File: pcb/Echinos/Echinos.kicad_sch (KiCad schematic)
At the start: 55 parts, among them J1 Conn_01x06_Socket, J10 TagConnect_6pins, J2 Conn_01x06_Socket, J3 Conn_01x06_Socket, J5 Conn_01x05_Socket, J6 USB_B_Micro, J7 Conn_01x04_Socket, J8 USB_C_Receptacle_USB2.0, J9 Conn_01x03_Socket, SW3 Reset, SW4 Reset, U1 Helios, U2 USBLC6-2P6, U3 XC6210B332MR-G, U7 USBLC6-2P6, U8 74LVC1T45

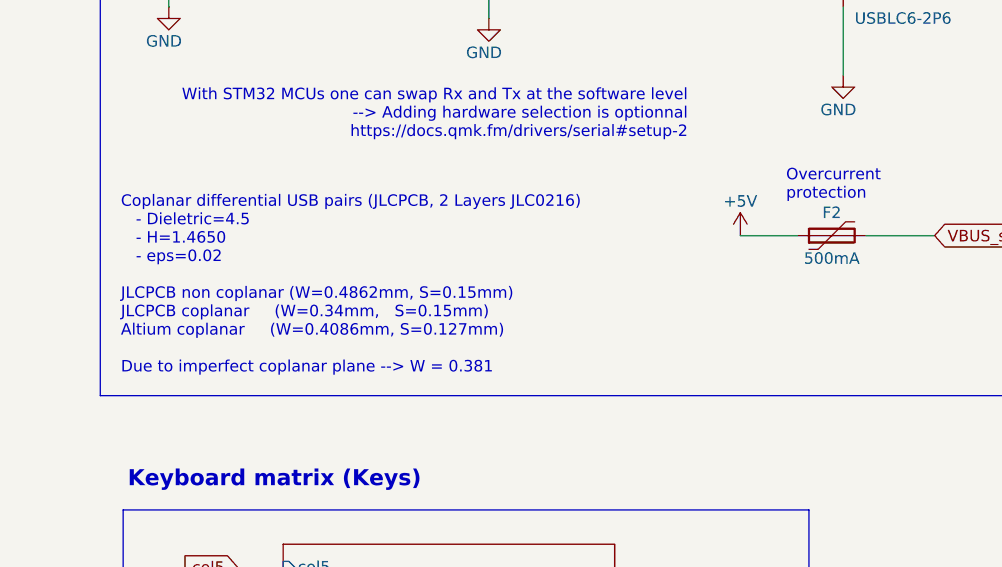
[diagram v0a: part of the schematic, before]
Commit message: [PCB] - Save last state with on board RP2040.   - Route crystal and 1V1
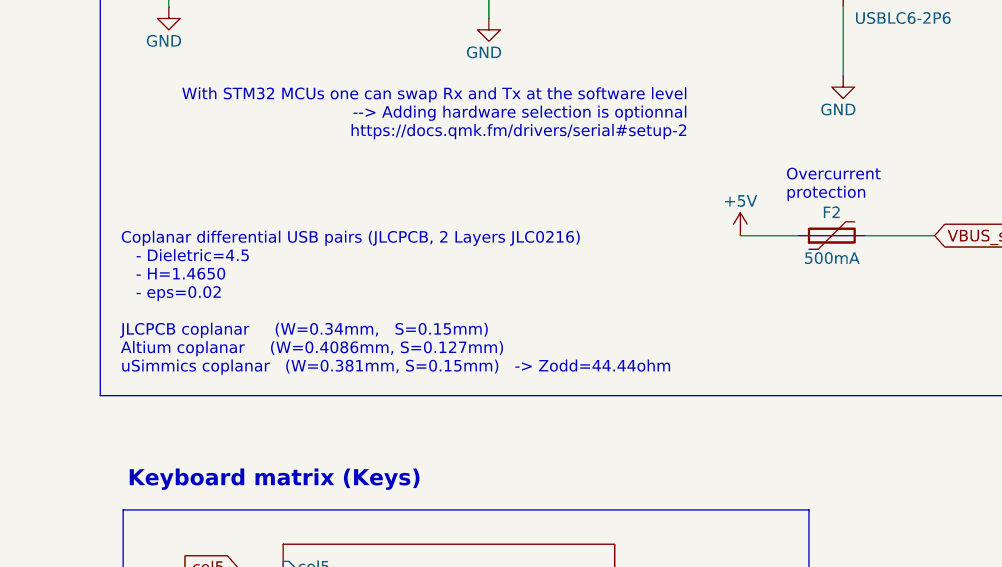
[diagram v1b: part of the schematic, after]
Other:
- note added: "Coplanar differential USB pairs (JLCPCB, 2 Layers JLC0216) - Dieletric=4.5 - H=1.4650 - eps=0.02 JLCPCB coplanar (W=0.34mm, S=0.15mm) Altium coplanar (W=0.4086mm, S=0.127mm) uSimmics coplanar (W=0.381mm, S=0.15mm) -> Zodd=44.44ohm"
- note removed: "Coplanar differential USB pairs (JLCPCB, 2 Layers JLC0216) - Dieletric=4.5 - H=1.4650 - eps=0.02 JLCPCB non coplanar (W=0.4862mm, S=0.15mm) JLCPCB coplanar (W=0.34mm, S=0.15mm) Altium coplanar (W=0.4086mm, S=0.127mm) Due to imperfect coplanar plane --> W = 0.381"
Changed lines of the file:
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@@
 		)
 	)
-	(text "Coplanar differential USB pairs (JLCPCB, 2 Layers JLC0216)\n   - Dieletric=4.5\n   - H=1.4650\n   - eps=0.02\n\nJLCPCB non coplanar (W=0.4862mm, S=0.15mm)\nJLCPCB coplanar     (W=0.34mm,   S=0.15mm)\nAltium coplanar     (W=0.4086mm, S=0.127mm)\n\nDue to imperfect coplanar plane --> W = 0.381"
+	(text "Coplanar differential USB pairs (JLCPCB, 2 Layers JLC0216)\n   - Dieletric=4.5\n   - H=1.4650\n   - eps=0.02\n\nJLCPCB coplanar     (W=0.34mm,   S=0.15mm)\nAltium coplanar     (W=0.4086mm, S=0.127mm) \nuSimmics coplanar   (W=0.381mm, S=0.15mm)   -> Zodd=44.44ohm"
 		(exclude_from_sim no)
 		(at 21.336 101.854 0)

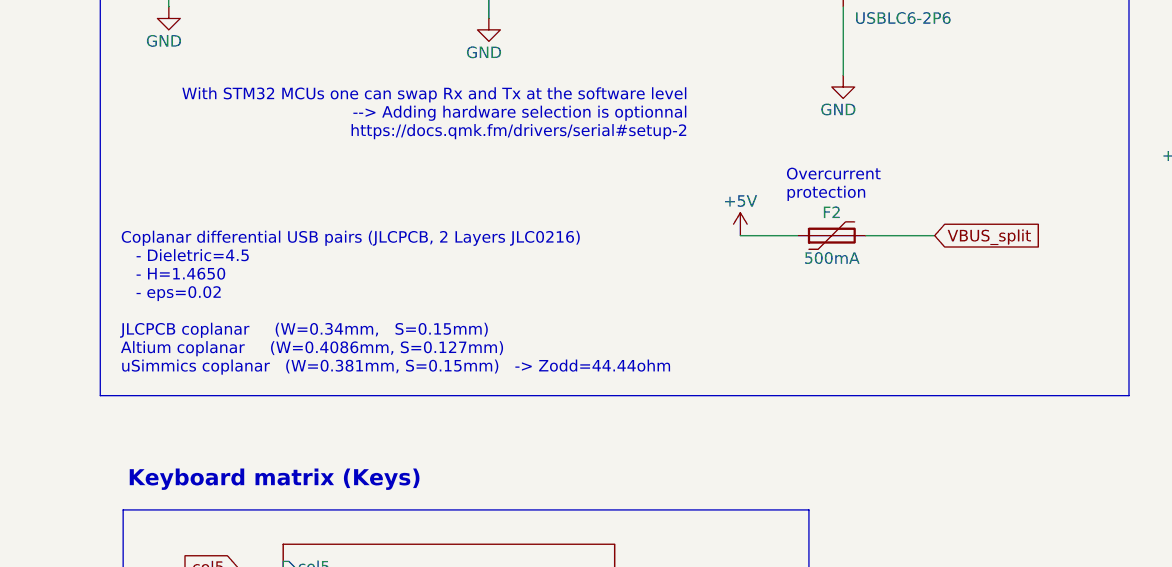
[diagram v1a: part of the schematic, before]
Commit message: [PCB] - Save last state with on board RP2040.   - Correct USB impedance   - Improve top plane grounding   - Add via at each layer switch   - Fix ERC issues   - Fix orientation / position of silkscreen
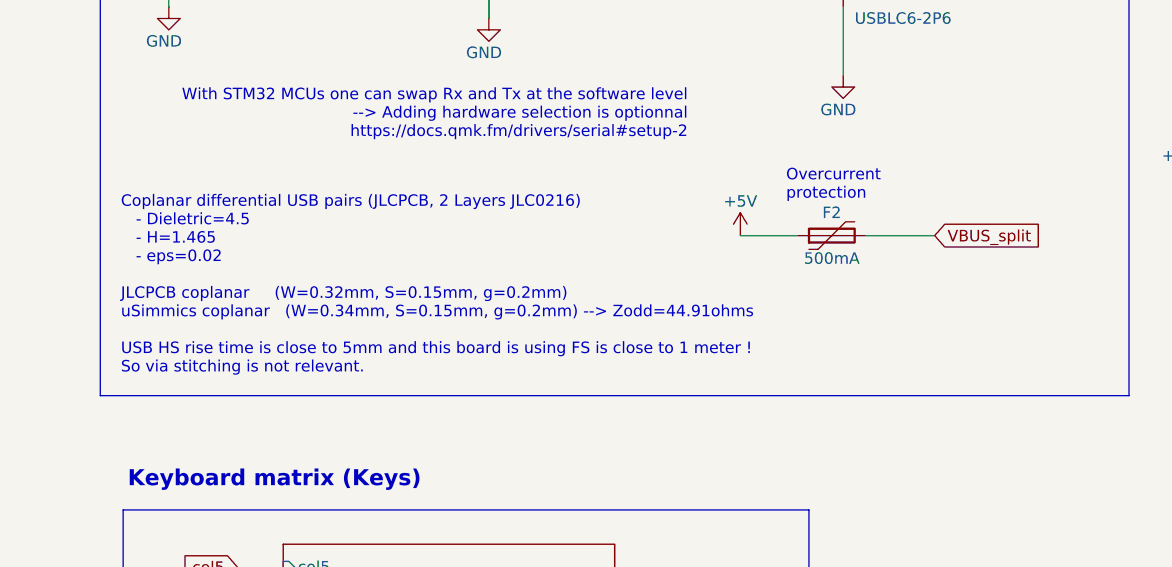
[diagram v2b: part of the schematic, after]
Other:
- note added: "Coplanar differential USB pairs (JLCPCB, 2 Layers JLC0216) - Dieletric=4.5 - H=1.465 - eps=0.02 JLCPCB coplanar (W=0.32mm, S=0.15mm, g=0.2mm) uSimmics coplanar (W=0.34mm, S=0.15mm, g=0.2mm) --> Zodd=44.91ohms USB HS rise time is close to 5mm and this board is using FS is close to 1 meter ! So via stitching is not relevant."
- note removed: "Coplanar differential USB pairs (JLCPCB, 2 Layers JLC0216) - Dieletric=4.5 - H=1.4650 - eps=0.02 JLCPCB coplanar (W=0.34mm, S=0.15mm) Altium coplanar (W=0.4086mm, S=0.127mm) uSimmics coplanar (W=0.381mm, S=0.15mm) -> Zodd=44.44ohm"
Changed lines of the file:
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@@
 		)
 	)
-	(text "Coplanar differential USB pairs (JLCPCB, 2 Layers JLC0216)\n   - Dieletric=4.5\n   - H=1.4650\n   - eps=0.02\n\nJLCPCB coplanar     (W=0.34mm,   S=0.15mm)\nAltium coplanar     (W=0.4086mm, S=0.127mm) \nuSimmics coplanar   (W=0.381mm, S=0.15mm)   -> Zodd=44.44ohm"
+	(text "Coplanar differential USB pairs (JLCPCB, 2 Layers JLC0216)\n   - Dieletric=4.5\n   - H=1.465\n   - eps=0.02\n\nJLCPCB coplanar     (W=0.32mm, S=0.15mm, g=0.2mm)\nuSimmics coplanar   (W=0.34mm, S=0.15mm, g=0.2mm) --> Zodd=44.91ohms\n\nUSB HS rise time is close to 5mm and this board is using FS is close to 1 meter !\nSo via stitching is not relevant."
 		(exclude_from_sim no)
 		(at 21.336 101.854 0)

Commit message: [PCB] - Save last state with on board RP2040.   - Clean schematics   - Fix flash capacitor value   - Fix flash schema to match all footprint pins   - Pass ERC (schema and pcb)   - Select missing LCSC components (USBC/B, buttons, vik connector)   - Add more margin to lateral pads in USB B footprint   - Improve top plane grounding under switches   - Adjust orientation and position to match JLCPCB   - Clean unused fields in schematics   - Add VIK connector footprint to lib (updated to match more models)   - Harmonization of footprints packaging for caps and resistors (either 0805 or 0402)   - Check availability and correctness of all parts   - Fix space in fields (was LCSC2 on leds)
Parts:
- removed J10: TagConnect_6pins, Connector:Tag-Connect_TC2030-IDC-FP_2x03_P1.27mm_Vertical, symbol Connector:Conn_ARM_SWD_TagConnect_TC2030
- removed J9: Conn_01x03_Socket, Connector_JST:JST_SH_BM03B-SRSS-TB_1x03-1MP_P1.00mm_Vertical, symbol Connector:Conn_01x03_Pin
- removed R18, R19: 100, Resistor_SMD:R_0805_2012Metric, symbol Device:R
- removed S2, S3, S4, S5, S6: GasketSupport, Echinos:EarCut_8mm, symbol Mechanical:Mechanical_Shape
- removed SW3, SW4: Reset, Button_Switch_SMD:SW_SPST_TS-1088-xR020, symbol Switch:SW_Push
- removed U1: Helios, Echinos:Helios_AH_USBup, symbol PCM_marbastlib-promicroish:Helios
- C1: value 1µ -> 1u; footprint Capacitor_SMD:C_0603_1608Metric_Pad1.08x0.95mm_HandSolder -> Capacitor_SMD:C_0805_2012Metric; LCSC C458913 -> C24123
- C2: value 4.7µ -> 1u; footprint Capacitor_SMD:C_0603_1608Metric_Pad1.08x0.95mm_HandSolder -> Capacitor_SMD:C_0805_2012Metric; LCSC C19666 -> C24123
- C3: MPN  10uF 20% 10V 0805 -> (none)
- D1: footprint Diode_SMD:D_SOD-323_HandSoldering -> LED_SMD:LED_0805_2012Metric; LCSC (none) -> C84260
- D3: MPN  B5817WS -> (none)
- FB1: MPN  BLM21AG601SH1D -> (none)
- J4: footprint Connector_FFC-FPC:Hirose_FH12-12S-0.5SH_1x12-1MP_P0.50mm_Horizontal -> Echinos:vik-keyboard-connector-horizontal; LCSC2 C3446010 -> C2906115; LCSC2_old_ (none) -> C3446010; LCSC_old (none) -> C479750
- J5: now left out of the parts list
- J6: Datasheet2 (none) -> https://www.lcsc.com/datasheet/C132562.pdf; Datasheet2_bis (none) -> https://fr.aliexpress.com/item/1005001673927357.html; Datasheet_bis (none) -> https://fr.aliexpress.com/item/1005007360060905.html; FT Position Offset (none) -> 0, 0.45; LCSC (none) -> C456008; LCSC2 (none) -> C132562
- J8: symbol Connector:USB_C_Receptacle_USB2.0 -> Connector:USB_C_Receptacle_USB2.0_16P; LCSC ??? C963373 ??? -> C3025063; MPN  ??? USB4510-03-1-A ??? -> (none)
- R12: MPN  5.1k 1% 0402 -> (none)
- R13, R14, R15, R16: footprint Resistor_SMD:R_0805_2012Metric_Pad1.20x1.40mm_HandSolder -> Resistor_SMD:R_0805_2012Metric
- R7, R8: MPN  5.1k 1% 0805 -> (none)
- R9: footprint Resistor_SMD:R_0402_1005Metric_Pad0.72x0.64mm_HandSolder -> Resistor_SMD:R_0805_2012Metric; LCSC C11702 -> C17513
- U2, U7: FT Rotation Offset (none) -> 90; MPN  USBLC6-2SC6 -> (none)
- U8: footprint Package_TO_SOT_SMD:SOT-563 -> Package_TO_SOT_SMD:SOT-23-6; JLCPCB_CORRECTION 0; 0; 270 -> (none); LCSC C352970 -> C7843; MPN  SN74LVC1T45DRLR -> (none)
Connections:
- no-connect marks 7 -> 5
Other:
- removed sheet Modules
- note added: "ESD protection (USB B)"
- note added: "Packaging (metric | imperial) - Resistors - RP2040 --> 1005 | 0402 - USB --> 1005 | 0402 - User --> 2012 | 0805 - LED --> 2012 | 0805 - Capacitors - RP2040 --> 1005 | 0402 - USB --> 2012 | 0805 - LED --> 2012 | 0805 - Diodes - Switches --> SOD-123 - TVS --> SOD-323"
- note added: "Special pins: - GPIO 00 et 01 is split communication - GPIO 24 is level shifted to 5V logic level (RGB) - GPIO 19 is VBUS detection - GPIO 12 is not connected / used - GPIO 18 is not connected / used"
- note removed: "Case Gasket mounts"
- note removed: "ESD protection (USB + SATA)"
- note removed: "Helios specific - GPIO 25 is level shifted to 5V logic level (RGB) - GPIO 19 is VBUS detection - GPIO 18 is not connected / used - GPIO 24 is not connected / used - GPIO 17 is micro LED (user controlled) - Power LED (Red) disabled by default (can be bridged)"
- note removed: "On board MCU reset"
- note removed: "Packaging (metric | imperial) - Resistors - RP2040 --> 1005 | 0402 - USB data --> 1005 | 0402 - I2C puller --> 1005 | 0402 - Others --> 1608 | 0603 - Capacitors - RP2040 --> 1005 | 0402 - Others --> 1608 | 0603 - Diodes - Switches --> SOD-123 - TVS --> SOD-523 - Transistors - ESD --> SOT-723"
- note removed: "Raspberry Pi Debug Probe"
- note removed: "Universal tag connector"
- moved on the sheet: C1, C2, C3, D1, D3, F2, F3, FB1, H1, H2, H3, H4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
